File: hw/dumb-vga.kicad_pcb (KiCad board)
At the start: 2 copper layers, 62.2 x 83.8 mm, 26 parts, among them IC1 74HC590N, IC2 74HC590N, IC3 74HC590N, IC4 74HC574N, P1 CONN_01X03, P2 CONN_01X03, P3 CONN_01X03, U1 A29040C, X1 VGAF

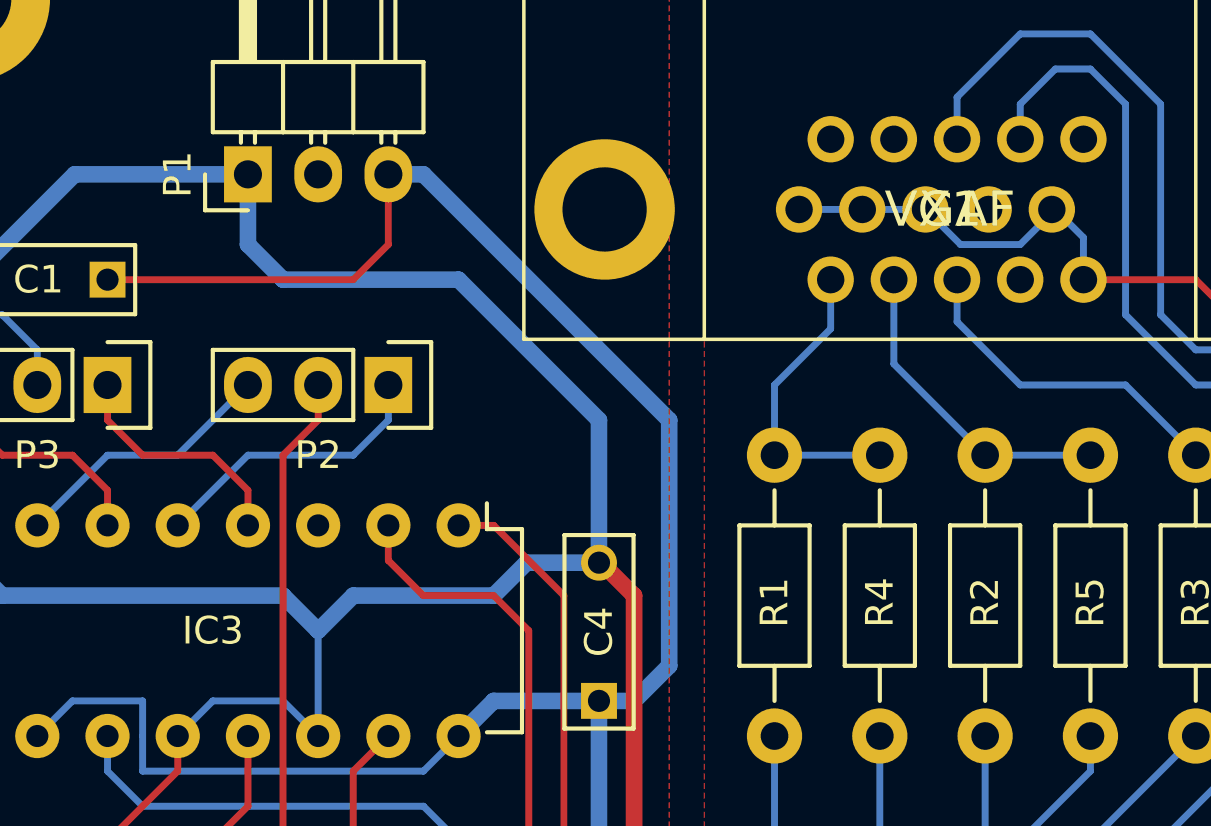
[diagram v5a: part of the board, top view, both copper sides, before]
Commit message: Update to new version of Kicad
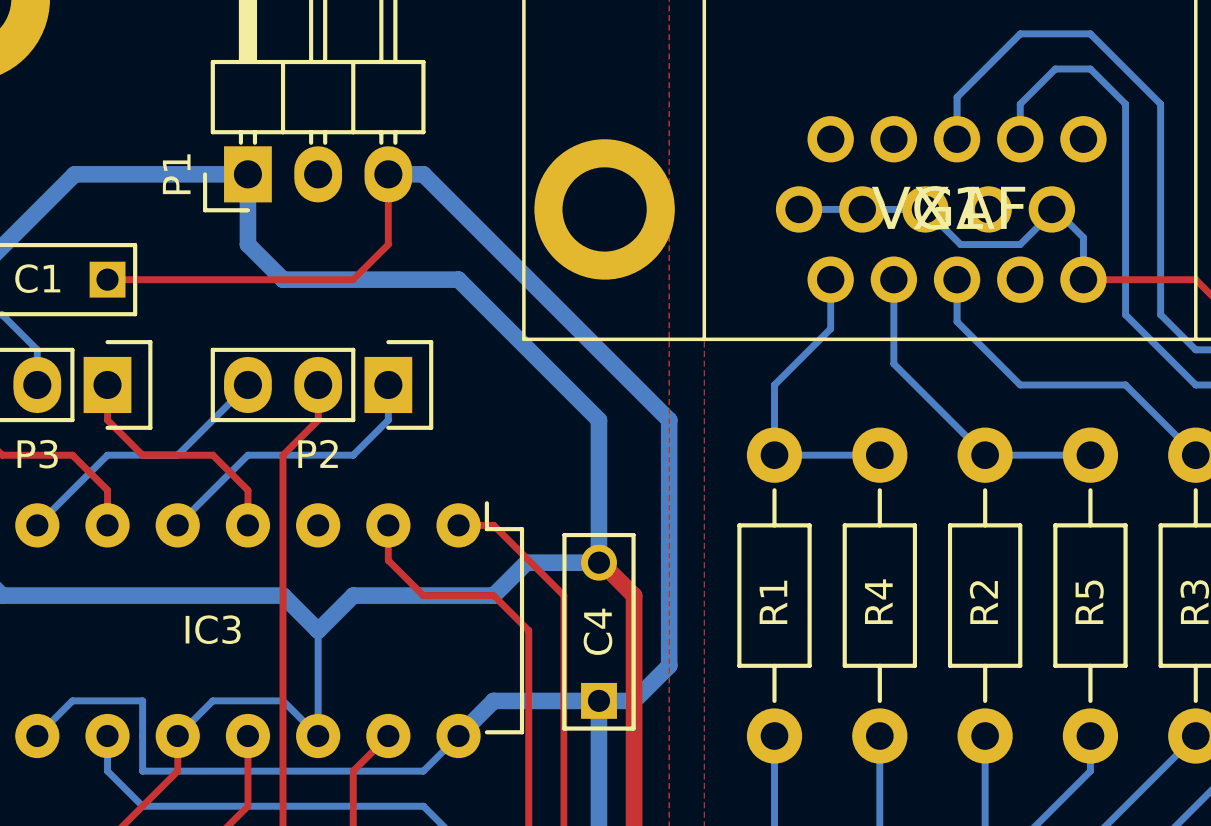
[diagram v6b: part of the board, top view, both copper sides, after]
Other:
- net class Default removed
- net class Power removed

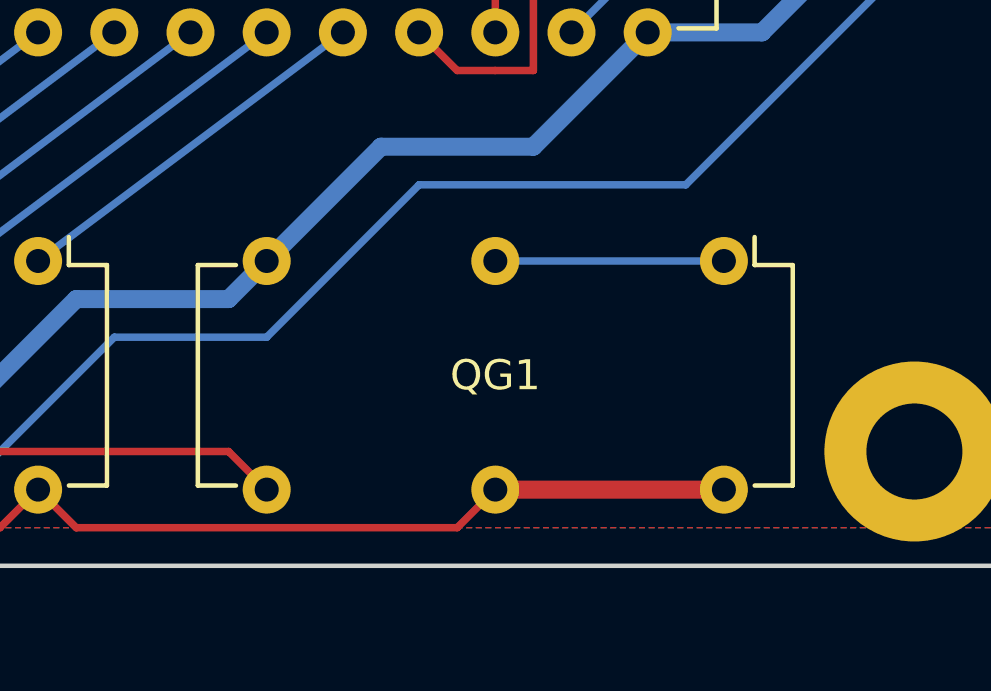
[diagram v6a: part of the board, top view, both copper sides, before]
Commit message: Move away from custom symbols, where convenient.
Upgrading from an ancient version of Kicad left me with a bunch of
symbosls in a local library that overlapped with the standard
library. For the easy cases, I've tried to switch over. Where it would
require rearranging lines on the schematic, I have not bothered.
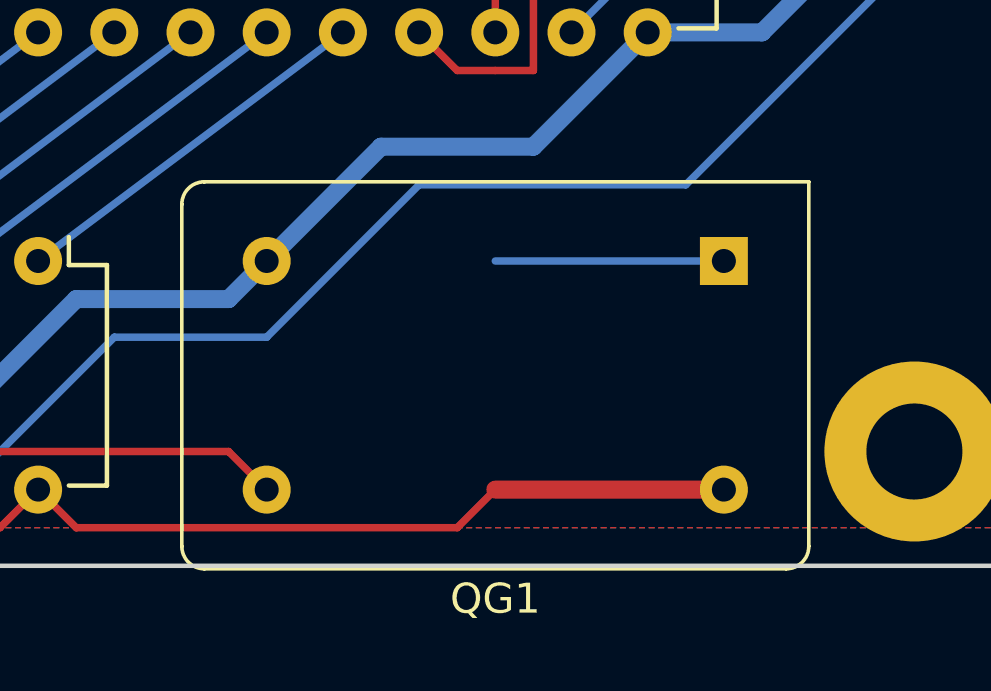
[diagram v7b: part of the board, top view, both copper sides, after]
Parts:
- QG1: footprint hw:xo-8-14 -> Oscillator:Oscillator_DIP-14
- R1, R2, R3: value 1.5K -> 680
- R4, R5, R6: value 680 -> 1.5K
- turned QG1 to 180 degrees
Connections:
- IC2 pad 2: (no net) -> unconnected-(IC2A-QC-Pad2)
- IC3 pad 3: (no net) -> unconnected-(IC3A-QD-Pad3)
- IC3 pad 9: (no net) -> unconnected-(IC3A-RCO-Pad9)
- P1 pad 2: (no net) -> unconnected-(P1-P2-Pad2)
- QG1 pad 1: Net-(QG1-Pad1) -> unconnected-(QG1-EN-Pad1)
- X1 pad 11: (no net) -> unconnected-(X1-P$11-Pad11)
- X1 pad 12: (no net) -> unconnected-(X1-P$12-Pad12)
- X1 pad 15: (no net) -> unconnected-(X1-P$15-Pad15)
- X1 pad 4: (no net) -> unconnected-(X1-P$4-Pad4)
- X1 pad 9: (no net) -> unconnected-(X1-P$9-Pad9)
- X1 pad SH1: (no net) -> unconnected-(X1-PadSH1)
- X1 pad SH2: (no net) -> unconnected-(X1-PadSH2)
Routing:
- net unconnected-(QG1-EN-Pad1): track 0.00 -> 7.62 mm
- net Net-(QG1-Pad1): track 7.62 -> 0.00 mm

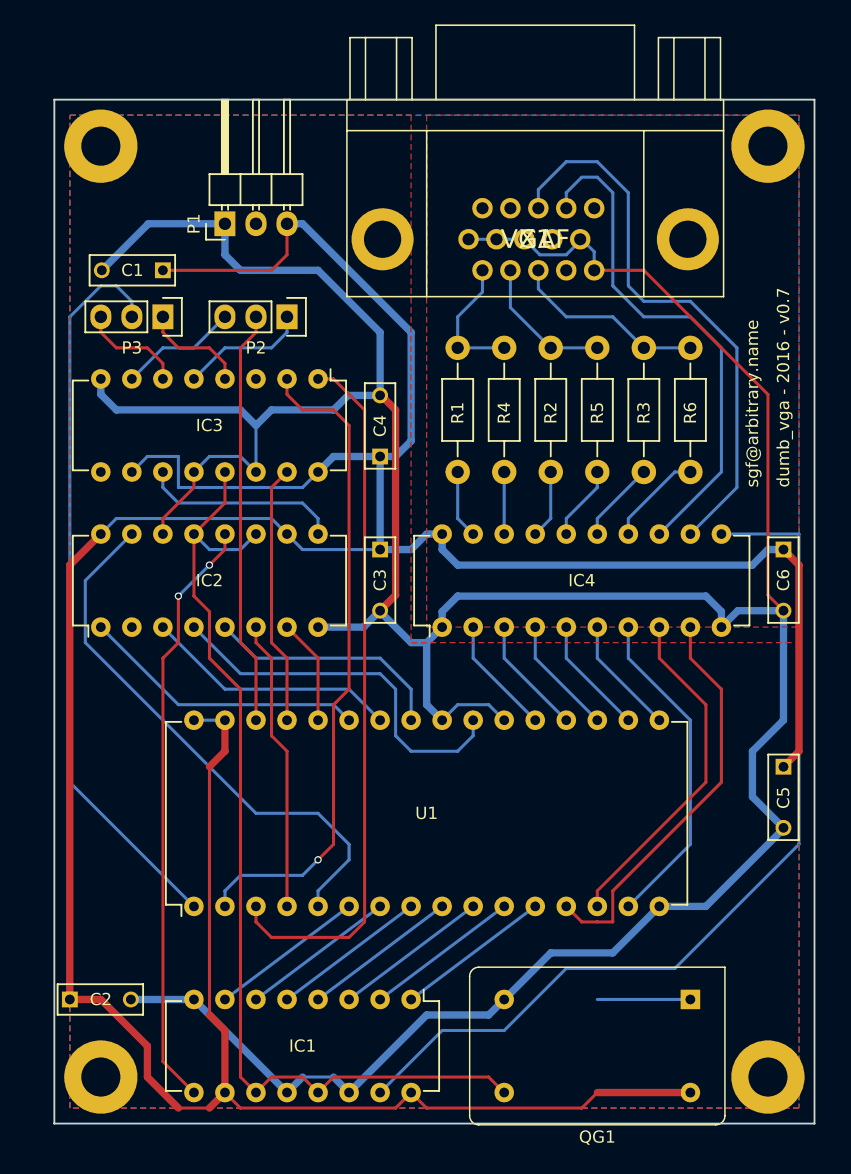
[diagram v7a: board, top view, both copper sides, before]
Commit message: Move PCB onto standard footprints
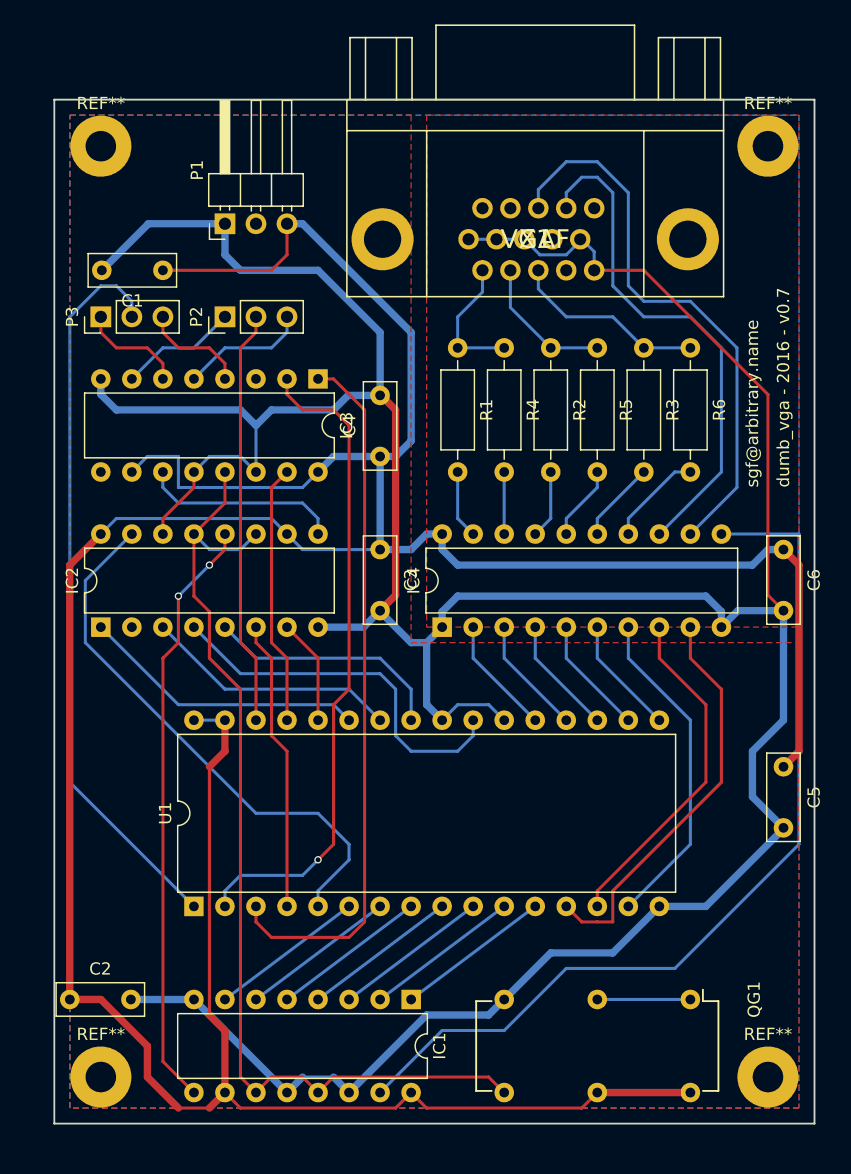
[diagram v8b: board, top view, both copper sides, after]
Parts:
- C1, C2, C3, C4, C5, C6: footprint Capacitors_ThroughHole:C_Rect_L7_W2.5_P5 -> Capacitor_THT:C_Rect_L7.0mm_W2.5mm_P5.00mm
- IC1, IC2, IC3: footprint Housings_DIP:DIP-16_W7.62mm -> Package_DIP:DIP-16_W7.62mm
- IC4: footprint Housings_DIP:DIP-20_W7.62mm -> Package_DIP:DIP-20_W7.62mm
- P1: footprint Pin_Headers:Pin_Header_Angled_1x03 -> Connector_PinHeader_2.54mm:PinHeader_1x03_P2.54mm_Horizontal
- P2, P3: footprint Pin_Headers:Pin_Header_Straight_1x03 -> Connector_PinHeader_2.54mm:PinHeader_1x03_P2.54mm_Vertical
- QG1: footprint Oscillator:Oscillator_DIP-14 -> hw:xo-8-14
- R1, R2, R3, R4, R5, R6: footprint Resistors_ThroughHole:Resistor_Horizontal_RM10mm -> Resistor_THT:R_Axial_DIN0207_L6.3mm_D2.5mm_P10.16mm_Horizontal
- REF** (x4): value SolderWirePad_single_2-5mmDrill -> MountingHole_2.5mm_Pad; footprint Wire_Pads:SolderWirePad_single_2-5mmDrill -> MountingHole:MountingHole_2.5mm_Pad
- U1: footprint Housings_DIP:DIP-32_W15.24mm -> Package_DIP:DIP-32_W15.24mm
- moved P2 5.08 mm to (118.1, 50.8), turned to 90 degrees
- moved P3 5.08 mm to (108.0, 50.8), turned to 90 degrees
- moved R1 5.08 mm to (137.2, 53.3)
- moved R2 5.08 mm to (144.8, 53.3)
- moved R3 5.08 mm to (152.4, 53.3)
- moved R4 5.08 mm to (141.0, 53.3)
- moved R5 5.08 mm to (148.6, 53.3)
- moved R6 5.08 mm to (156.2, 53.3)
- turned QG1 to -90 degrees
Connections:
- P2 pad 1: Net-(IC3A-QF) -> Net-(IC3A-QH)
- P2 pad 3: Net-(IC3A-QH) -> Net-(IC3A-QF)
- P3 pad 1: Net-(IC3A-QE) -> Net-(IC3A-QG)
- P3 pad 3: Net-(IC3A-QG) -> Net-(IC3A-QE)
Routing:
- net GND: track 289.7 -> 290.5 mm
